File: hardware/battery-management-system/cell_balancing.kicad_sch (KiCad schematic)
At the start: 42 parts, among them J23 Conn_01x05, Q16 DMN3404L, Q17 DMN3404L, Q18 DMN3404L, Q19 DMN3404L, Q2 TJ40S04M3L, Q20 DMN3404L, Q21 DMN3404L, Q22 DMN3404L, Q23 DMN3404L, Q24 DMN3404L, Q25 DMN3404L, Q26 DMN3404L, Q27 DMN3404L, Q28 DMN3404L, Q29 DMN3404L, Q30 DMN3404L, Q31 DMN3404L, Q32 DMN3404L, Q33 DMN3404L, Q34 DMN3404L, Q35 DMN3404L, Q36 DMN3404L, Q37 DMN3404L, Q38 DMN3404L, Q39 DMN3404L, U13 MC74VHC139

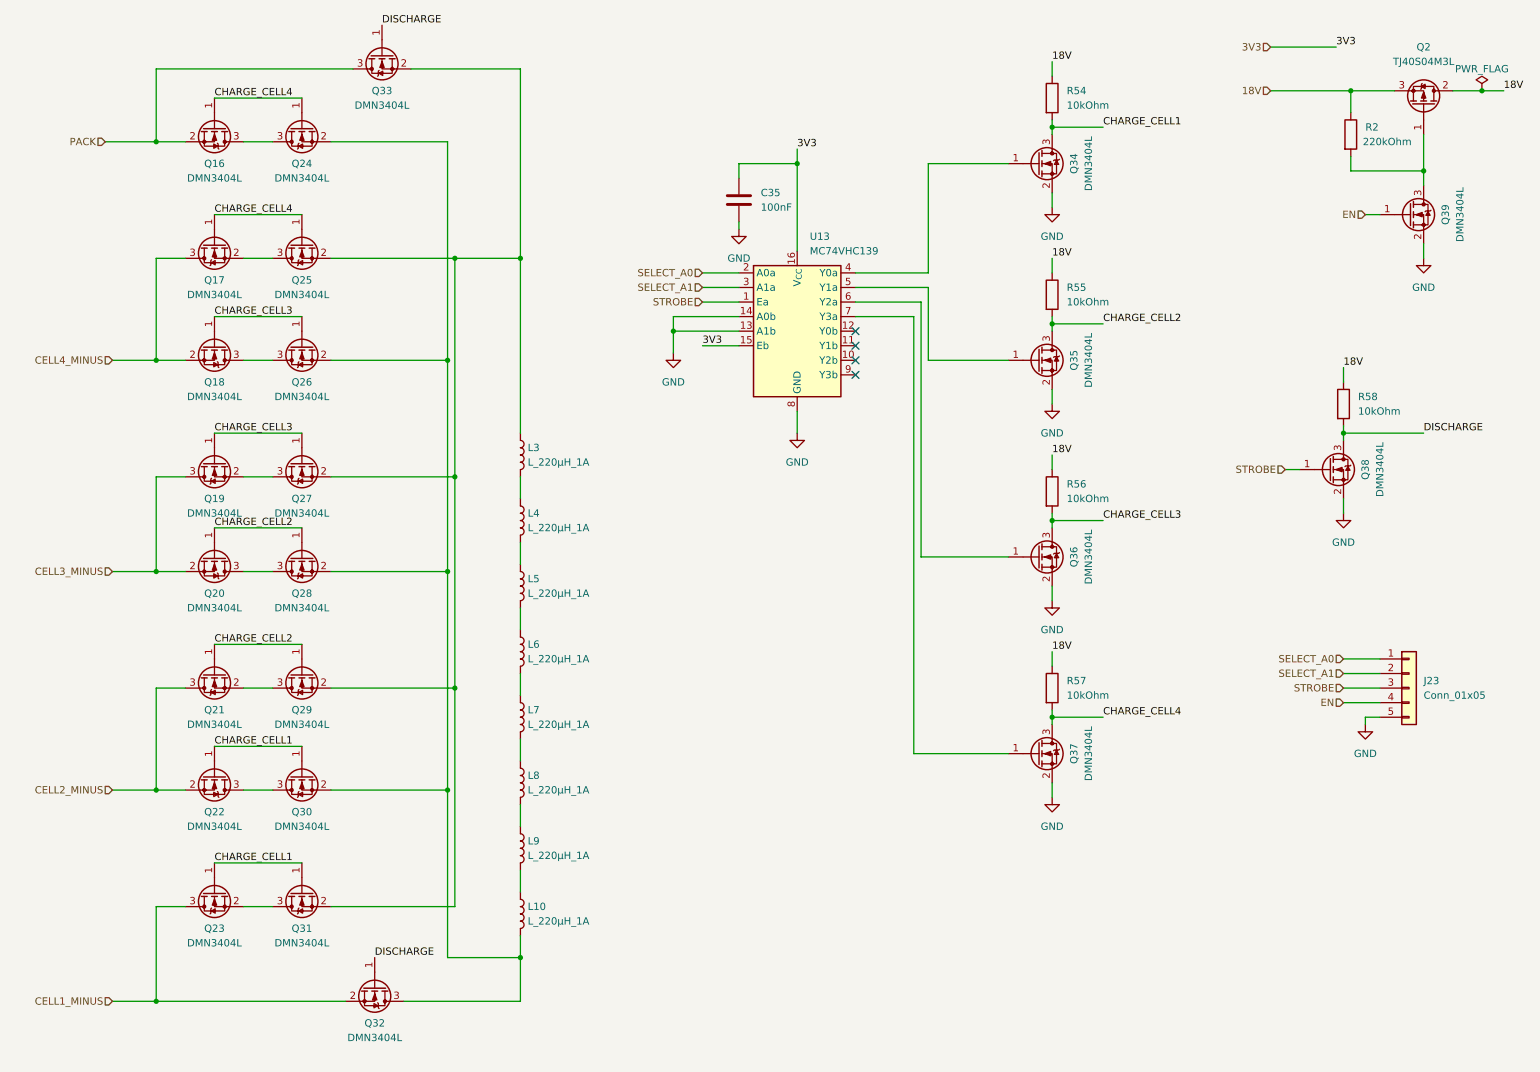
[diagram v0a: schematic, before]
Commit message: add fuel gauge to BMS
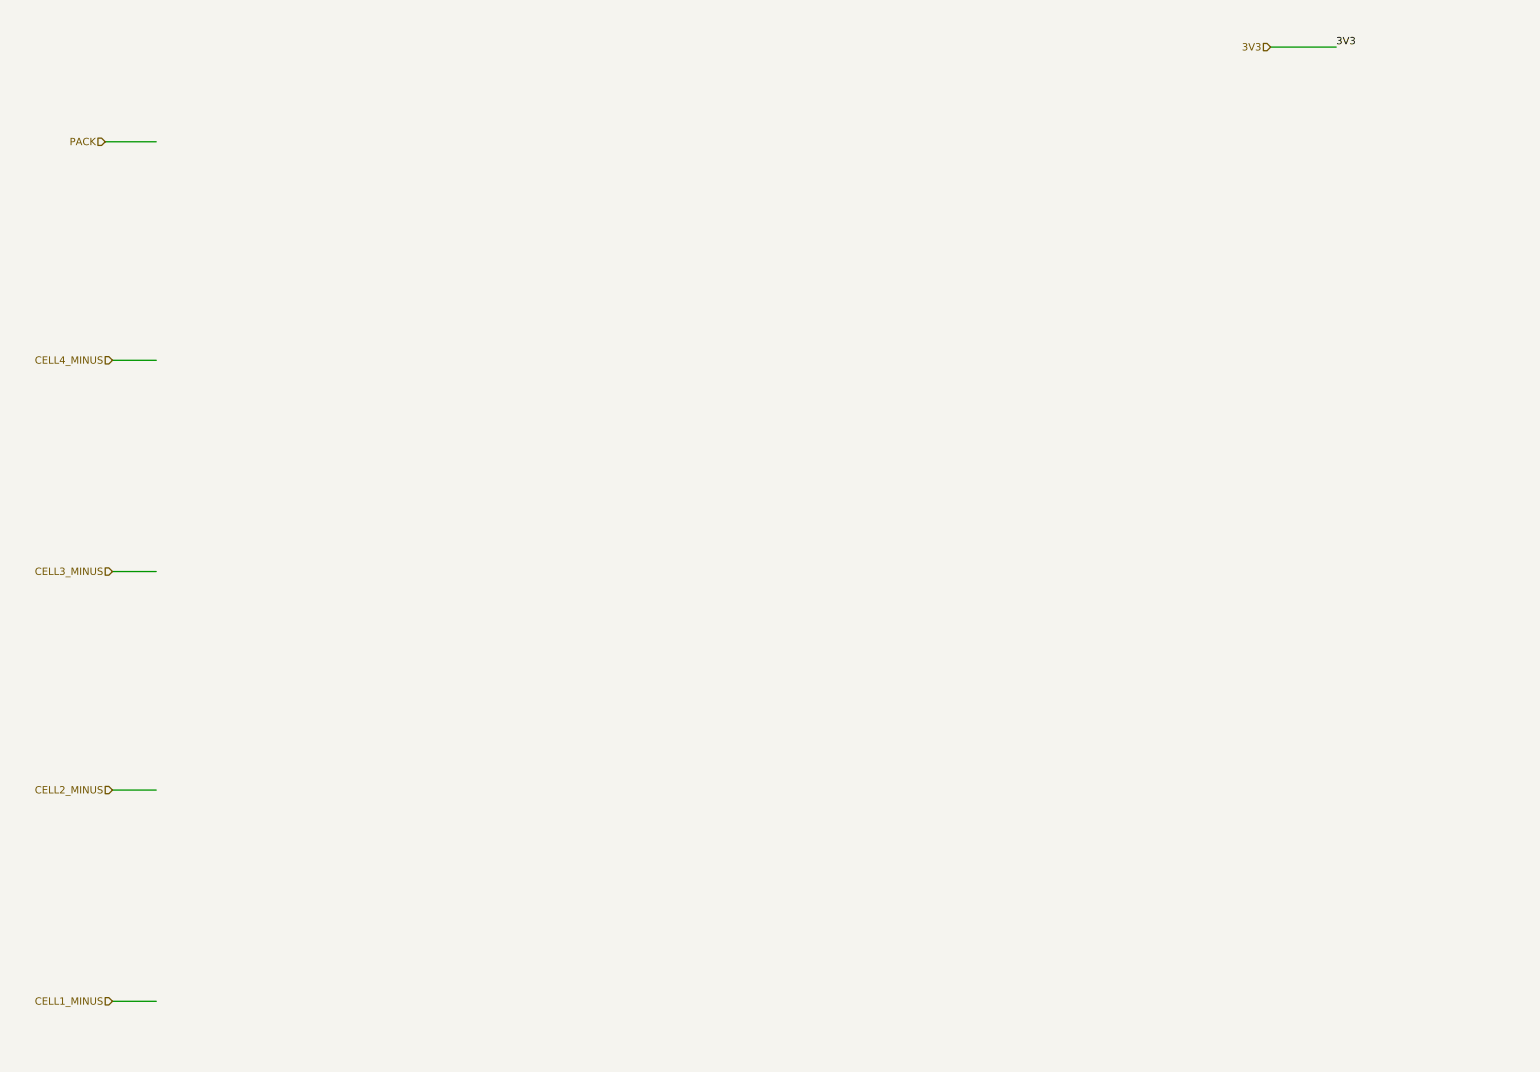
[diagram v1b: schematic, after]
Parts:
- removed C35: 100nF, benediktibk:C_0603_1608Metric_Pad1.08x0.95mm_HandSolder, symbol benediktibk:C_100nF_SMD_0603_50V
- removed J23: Conn_01x05, benediktibk:PinHeader_1x05_P2.54mm_Vertical, symbol benediktibk:Conn_01x05
- removed L10, L3, L4, L5, L6, L7, L8, L9: L_220µH_1A, benediktibk:L_Wuerth_HCI-1050, symbol benediktibk:L_220µH_1A
- removed Q16, Q17, Q18, Q19, Q20, Q21, Q22, Q23, Q24, Q25, Q26, Q27, Q28, Q29, Q30, Q31, Q32, Q33, Q34, Q35, Q36, Q37, Q38, Q39: DMN3404L, benediktibk:SOT-23, symbol benediktibk:DMN3404L
- removed Q2: TJ40S04M3L, benediktibk:TO-252-2, symbol benediktibk:TJ40S04M3L
- removed R2: 220kOhm, benediktibk:R_0603_1608Metric_Pad0.98x0.95mm_HandSolder, symbol benediktibk:R_220kOhm_SMD_0603_100mW_1%
- removed R54, R55, R56, R57, R58: 10kOhm, benediktibk:R_0603_1608Metric_Pad0.98x0.95mm_HandSolder, symbol benediktibk:R_10kOhm_SMD_0603_100mW_1%
- removed U13: MC74VHC139, benediktibk:TSSOP-16_4.4x5mm_P0.65mm, symbol benediktibk:MC74VHC139
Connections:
- no-connect marks 4 -> 0

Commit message: start with cell balancing in BMS
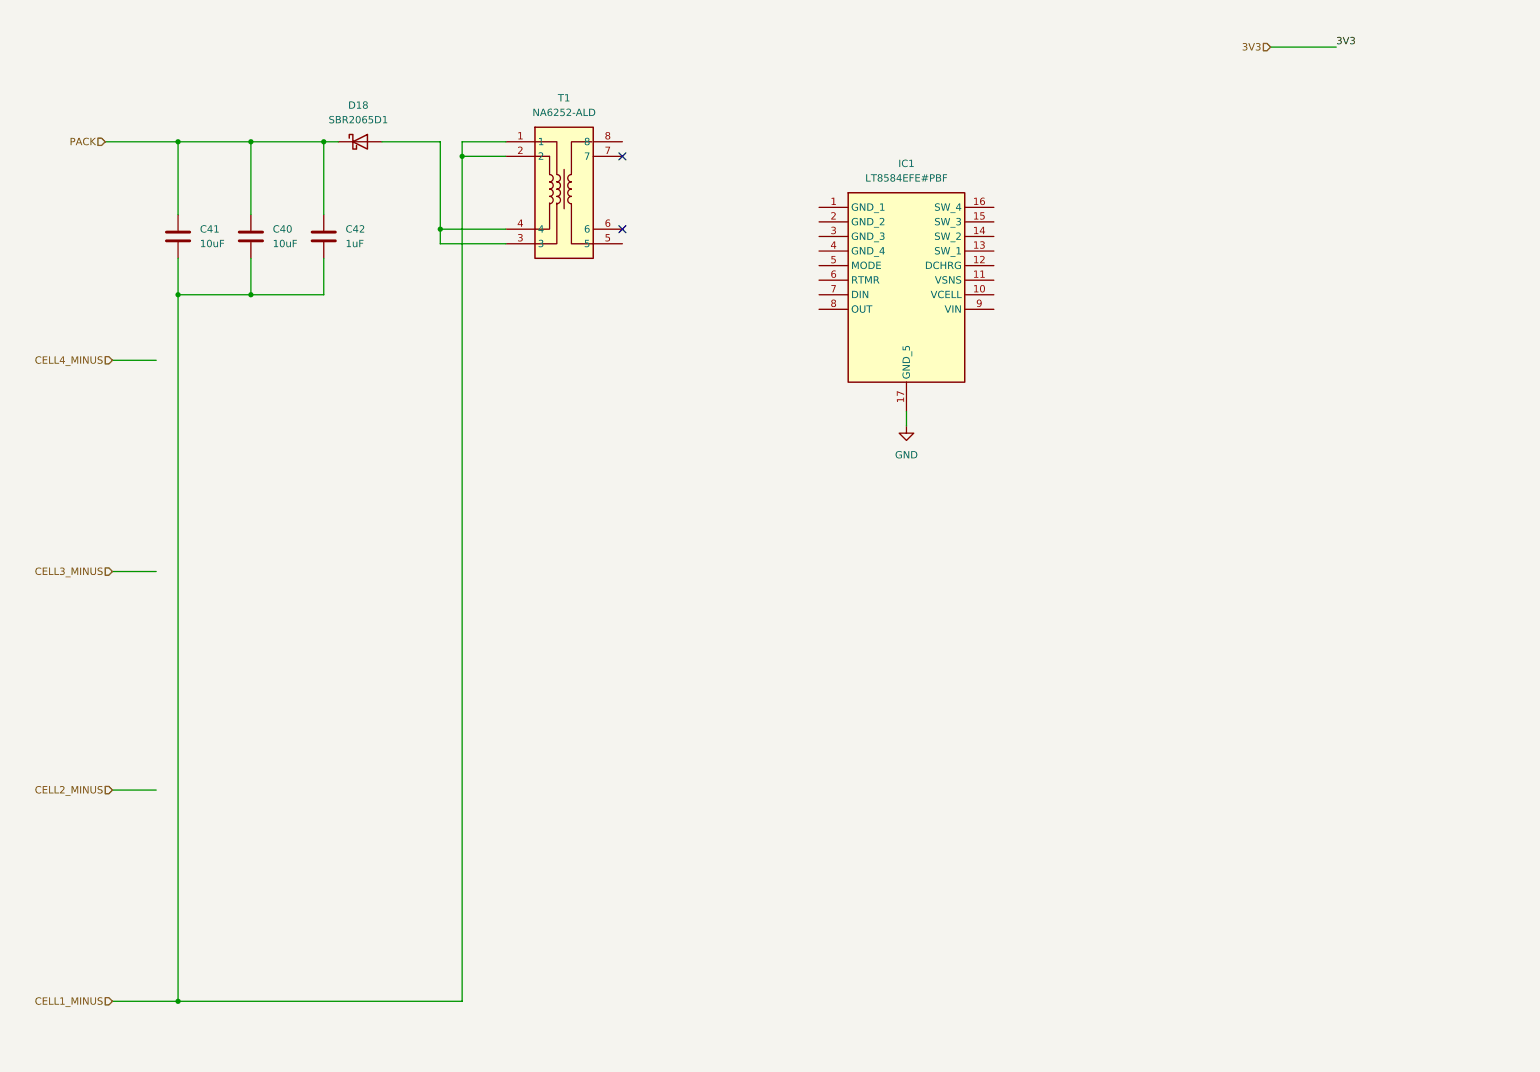
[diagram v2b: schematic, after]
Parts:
- added C40, C41: 10uF, benediktibk:C_1210_3225Metric_Pad1.33x2.70mm_HandSolder, symbol benediktibk:C_10uF_SMD_1210_50V_20%
- added C42: 1uF, benediktibk:C_0603_1608Metric_Pad1.08x0.95mm_HandSolder, symbol benediktibk:C_1uF_SMD_0603_50V_10%
- added D18: SBR2065D1, benediktibk:SBR2065D1, symbol benediktibk:SBR2065D1
- added IC1: LT8584EFE#PBF, benediktibk:SOP65P640X110-17N, symbol benediktibk:LT8584EFE#PBF
- added T1: NA6252-ALD, benediktibk:SOP250P1524X1143-8N, symbol benediktibk:NA6252-ALD
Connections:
- net CELL1_MINUS: now also C40.2, C41.2, C42.2, T1.1, T1.2
- net PACK: now also C40.1, C41.1, C42.1, D18.2 (K)
- new net: D18.1 (A), T1.3, T1.4
- new net GND: IC1.17 (GND_5)
- no-connect marks 0 -> 2

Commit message: finish cell balancing schematic
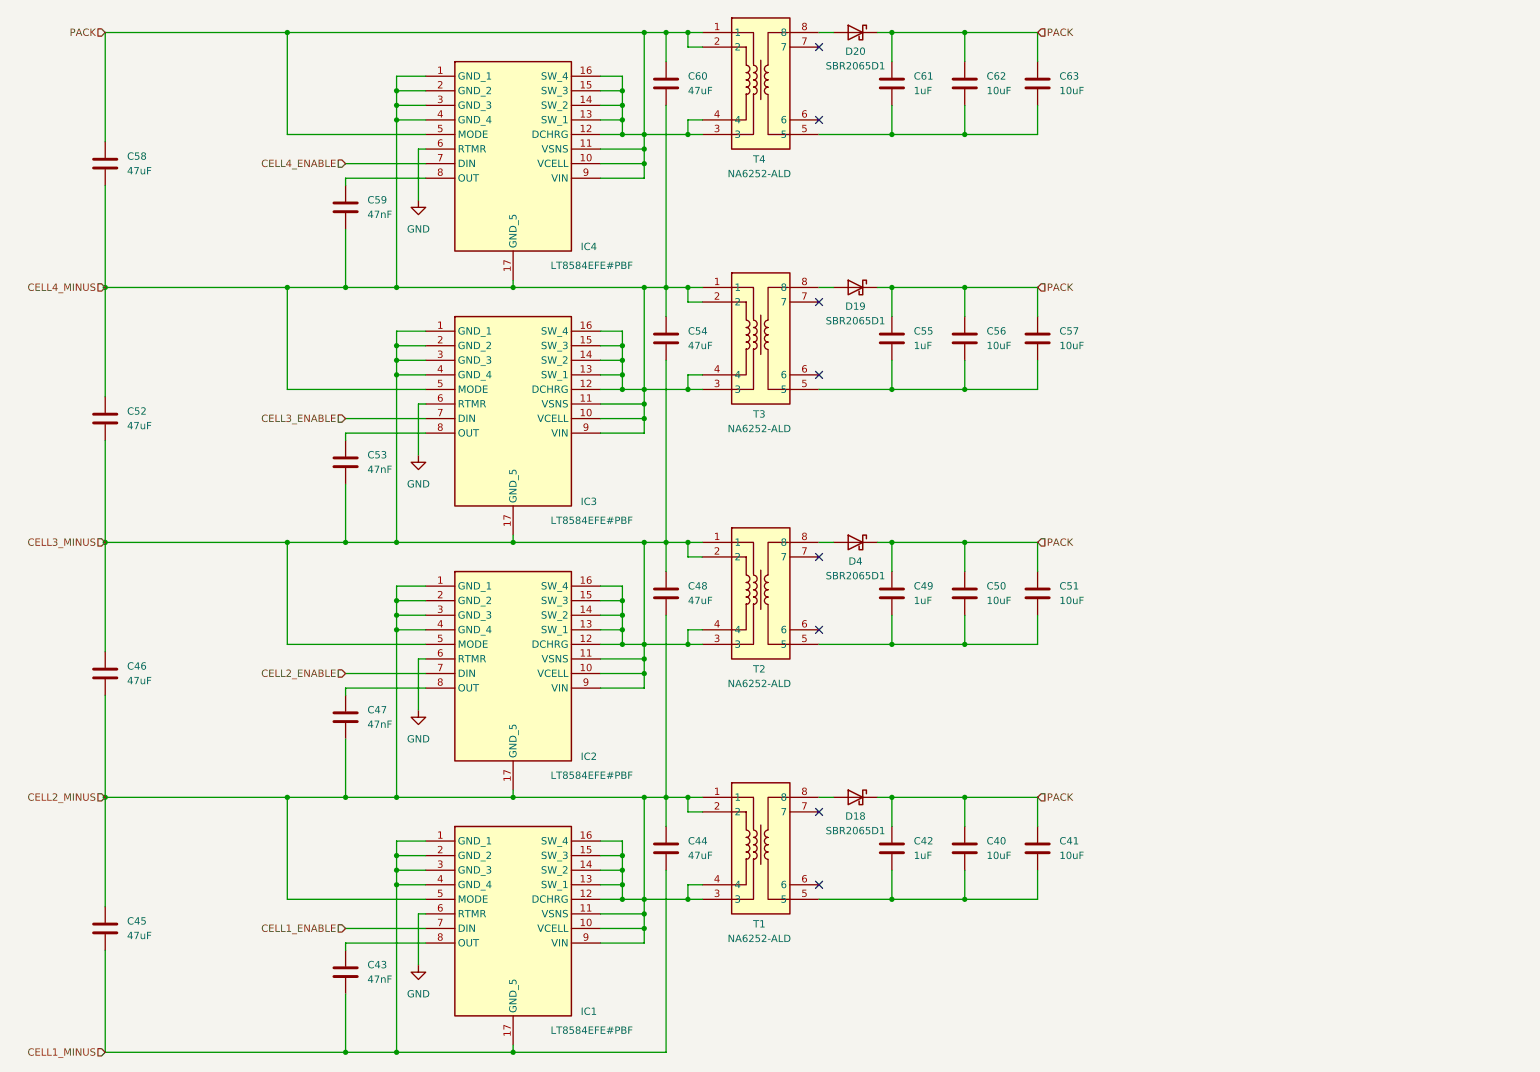
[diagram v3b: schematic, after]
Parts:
- added C43, C47, C53, C59: 47nF, benediktibk:C_0603_1608Metric_Pad1.08x0.95mm_HandSolder, symbol benediktibk:C_47nF_SMD_0603_16V_10%
- added C44, C45, C46, C48, C52, C54, C58, C60: 47uF, benediktibk:C_1206_3216Metric_Pad1.33x1.80mm_HandSolder, symbol benediktibk:C_47uF_SMD_1206_25V_20%
- added C49, C55, C61: 1uF, benediktibk:C_0603_1608Metric_Pad1.08x0.95mm_HandSolder, symbol benediktibk:C_1uF_SMD_0603_50V_10%
- added C50, C51, C56, C57, C62, C63: 10uF, benediktibk:C_1210_3225Metric_Pad1.33x2.70mm_HandSolder, symbol benediktibk:C_10uF_SMD_1210_50V_20%
- added D19, D20, D4: SBR2065D1, benediktibk:SBR2065D1, symbol benediktibk:SBR2065D1
- added IC2, IC3, IC4: LT8584EFE#PBF, benediktibk:SOP65P640X110-17N, symbol benediktibk:LT8584EFE#PBF
- added T2, T3, T4: NA6252-ALD, benediktibk:SOP250P1524X1143-8N, symbol benediktibk:NA6252-ALD
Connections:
- net CELL1_MINUS: now also IC1.1 (GND_1), IC1.17 (GND_5), IC1.2 (GND_2), IC1.3 (GND_3), IC1.4 (GND_4), C43.2, C44.2, C45.2; no longer C40.2, C41.2, C42.2, T1.1, T1.2
- net CELL2_MINUS: now also IC1.10 (VCELL), IC1.11 (VSNS), IC1.12 (DCHRG), IC1.13 (SW_1), IC1.14 (SW_2), IC1.15 (SW_3), IC1.16 (SW_4), IC1.5 (MODE), IC1.9 (VIN), T1.1, T1.2, T1.3, T1.4, C44.1, C45.1, C46.2, C47.2, C48.2, IC2.1 (GND_1), IC2.17 (GND_5), IC2.2 (GND_2), IC2.3 (GND_3), IC2.4 (GND_4)
- net CELL3_MINUS: now also C46.1, C48.1, C52.2, C53.2, C54.2, IC2.10 (VCELL), IC2.11 (VSNS), IC2.12 (DCHRG), IC2.13 (SW_1), IC2.14 (SW_2), IC2.15 (SW_3), IC2.16 (SW_4), IC2.5 (MODE), IC2.9 (VIN), IC3.1 (GND_1), IC3.17 (GND_5), IC3.2 (GND_2), IC3.3 (GND_3), IC3.4 (GND_4), T2.1, T2.2, T2.3, T2.4
- net CELL4_MINUS: now also C52.1, C54.1, C58.2, C59.2, C60.2, IC3.10 (VCELL), IC3.11 (VSNS), IC3.12 (DCHRG), IC3.13 (SW_1), IC3.14 (SW_2), IC3.15 (SW_3), IC3.16 (SW_4), IC3.5 (MODE), IC3.9 (VIN), IC4.1 (GND_1), IC4.17 (GND_5), IC4.2 (GND_2), IC4.3 (GND_3), IC4.4 (GND_4), T3.1, T3.2, T3.3, T3.4
- net GND: now also IC1.6 (RTMR), IC2.6 (RTMR), IC3.6 (RTMR), IC4.6 (RTMR); no longer IC1.17 (GND_5)
- net PACK: now also C49.1, C50.1, C51.1, C55.1, C56.1, C57.1, C58.1, C60.1, C61.1, C62.1, C63.1, D19.2 (K), D20.2 (K), D4.2 (K), IC4.10 (VCELL), IC4.11 (VSNS), IC4.12 (DCHRG), IC4.13 (SW_1), IC4.14 (SW_2), IC4.15 (SW_3), IC4.16 (SW_4), IC4.5 (MODE), IC4.9 (VIN), T4.1, T4.2, T4.3, T4.4
- net at T1.5: now also C40.2, C41.2, C42.2
- net at T1.8: now also D18.1 (A)
- net CELL1_ENABLE: now reaches IC1.7 (DIN)
- net at IC1.8 (OUT): now also C43.1
- new net: C59.1, IC4.8 (OUT)
- new net: C49.2, C50.2, C51.2, T2.5
- new net: C61.2, C62.2, C63.2, T4.5
- new net: D20.1 (A), T4.8
- new net: C55.2, C56.2, C57.2, T3.5
- new net: D19.1 (A), T3.8
- new net: D4.1 (A), T2.8
- new net: C47.1, IC2.8 (OUT)
- new net: C53.1, IC3.8 (OUT)
- new net CELL2_ENABLE: IC2.7 (DIN)
- new net CELL3_ENABLE: IC3.7 (DIN)
- new net CELL4_ENABLE: IC4.7 (DIN)
- no-connect marks 2 -> 8
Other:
- moved on the sheet: C40, C41, C42, D18, IC1, T1

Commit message: add snubber circuit
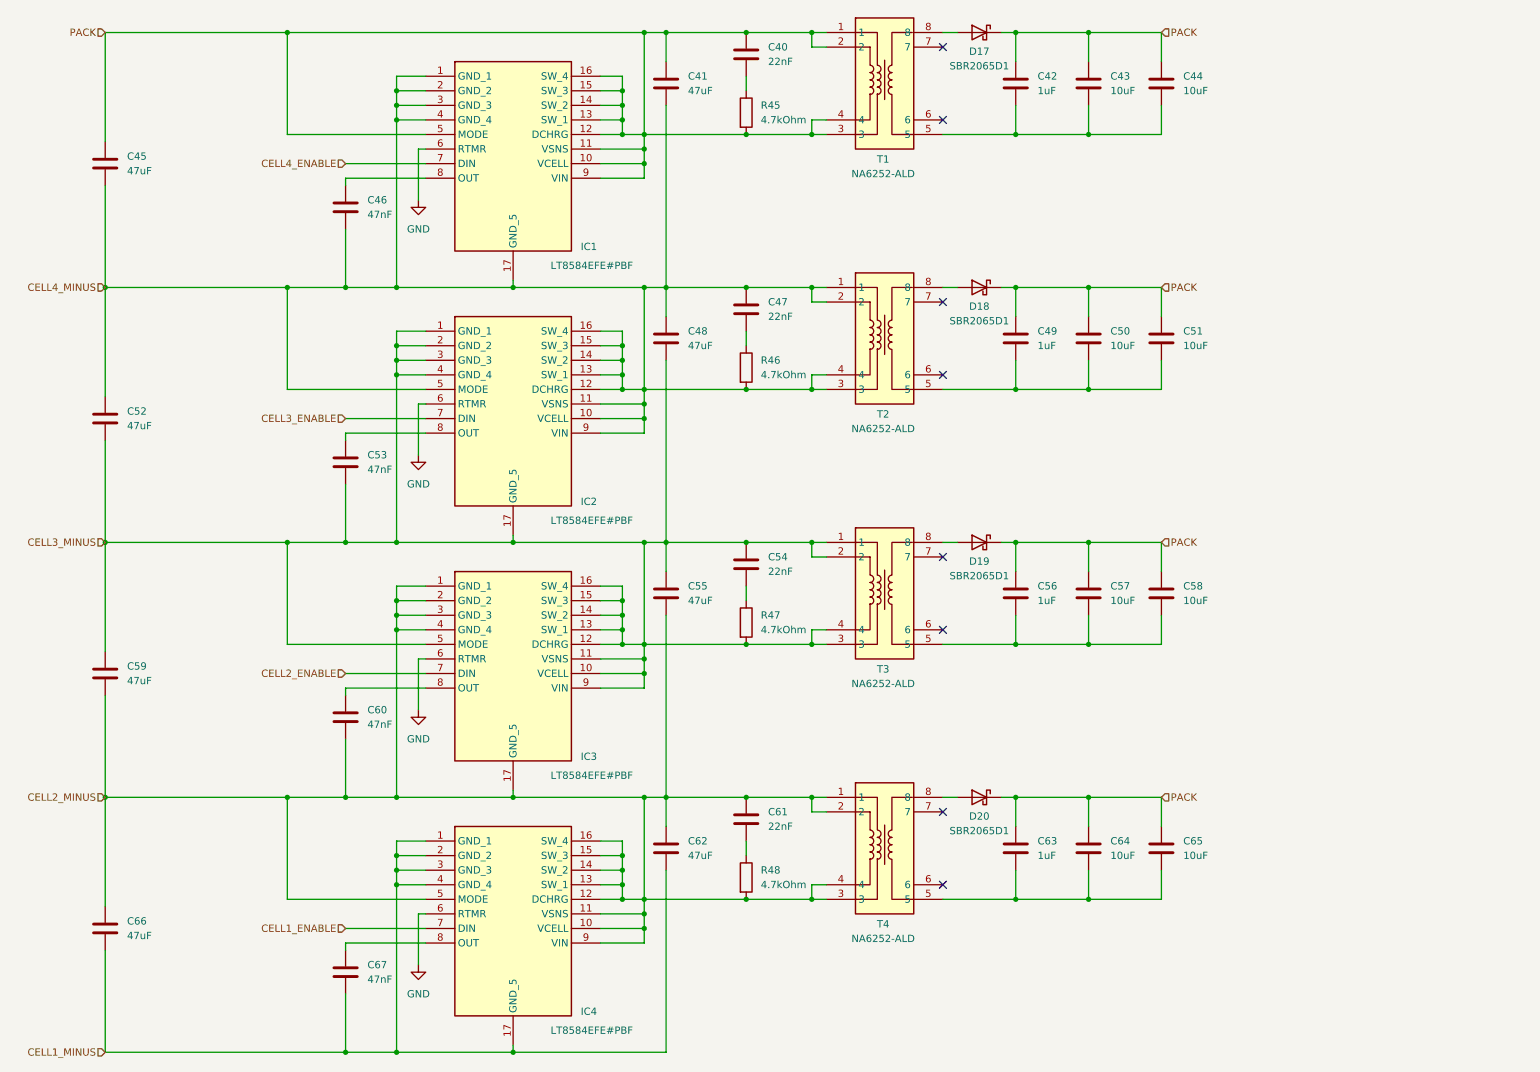
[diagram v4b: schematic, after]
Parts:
- added C40, C47, C54, C61: 22nF, benediktibk:C_0603_1608Metric_Pad1.08x0.95mm_HandSolder, symbol benediktibk:C_22nF_SMD_0603_16V_10%
- added R45, R46, R47, R48: 4.7kOhm, benediktibk:R_0603_1608Metric_Pad0.98x0.95mm_HandSolder, symbol benediktibk:R_4_7kOhm_SMD_0603_100mW_1%
- renumbered C60 to C41, C61 to C42, C62 to C43, C63 to C44, C58 to C45, C59 to C46, C54 to C48, C55 to C49, C56 to C50, C57 to C51, C48 to C55, C49 to C56, C50 to C57, C51 to C58, C46 to C59, C47 to C60, C44 to C62, C42 to C63, C40 to C64, C41 to C65, C45 to C66, C43 to C67, D20 to D17, D19 to D18, D4 to D19, D18 to D20, IC4 to IC1, IC3 to IC2, IC2 to IC3, IC1 to IC4, T4 to T1, T3 to T2, T2 to T3, T1 to T4
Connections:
- net CELL2_MINUS: now also C61.1, R48.2
- net CELL3_MINUS: now also C54.1, R47.2
- net CELL4_MINUS: now also C47.1, R46.2
- net PACK: now also C40.1, R45.2
- new net: C47.2, R46.1
- new net: C40.2, R45.1
- new net: C54.2, R47.1
- new net: C61.2, R48.1
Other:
- moved on the sheet: C42, C43, C44, C49, C50, C51, C56, C57, C58, C63, C64, C65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
